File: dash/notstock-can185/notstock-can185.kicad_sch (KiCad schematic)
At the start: 29 parts, among them J1 OBD 12V GND H L, J2 UART wires from display, J3 BAT to display, U1 LMR16006YDDCR, U2 SN65HVD230

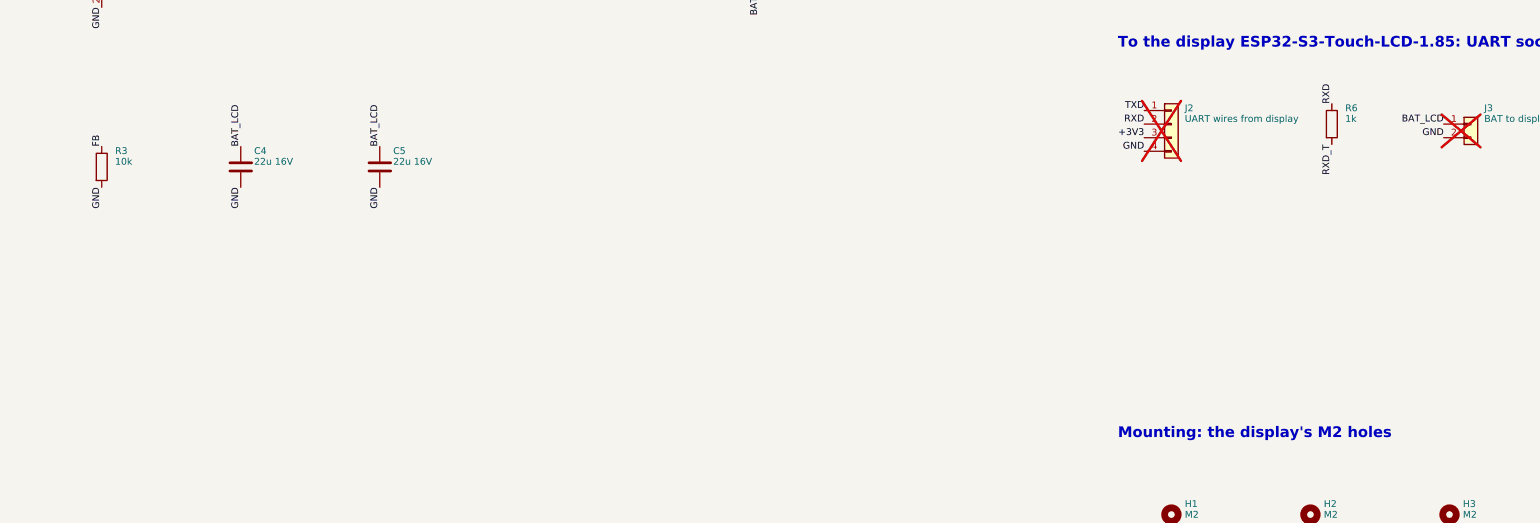
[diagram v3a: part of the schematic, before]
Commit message: CAN 1.85 rev 7: LC filter on the display's supply, JST XH for J1
Rev 6 in the car: the display's touch needed a hard press. A second LC
stage after the regulator (L2 1 uH, C9 C10 22 uF, C11 100 nF), its
corner about 30 kHz, keeps the 2.1 MHz ripple some 70 dB lower off the
display; the feedback stays before it. L2 about 12 mm from L1.

J1 is a JST XH 2.5 mm (B4B-XH-A, C144395, through hole): bigger crimps
than the PH, ready-made leads. The T5 vent's lid has its window moved
and grown for it. Readable schematic: D1 and D3 named as fitted.

Co-Authored-By: Claude Opus 5.5 <noreply@anthropic.com>
Claude-Session: https://claude.ai/code/session_018SKN4tJhAPpVCWtvRZgZpD
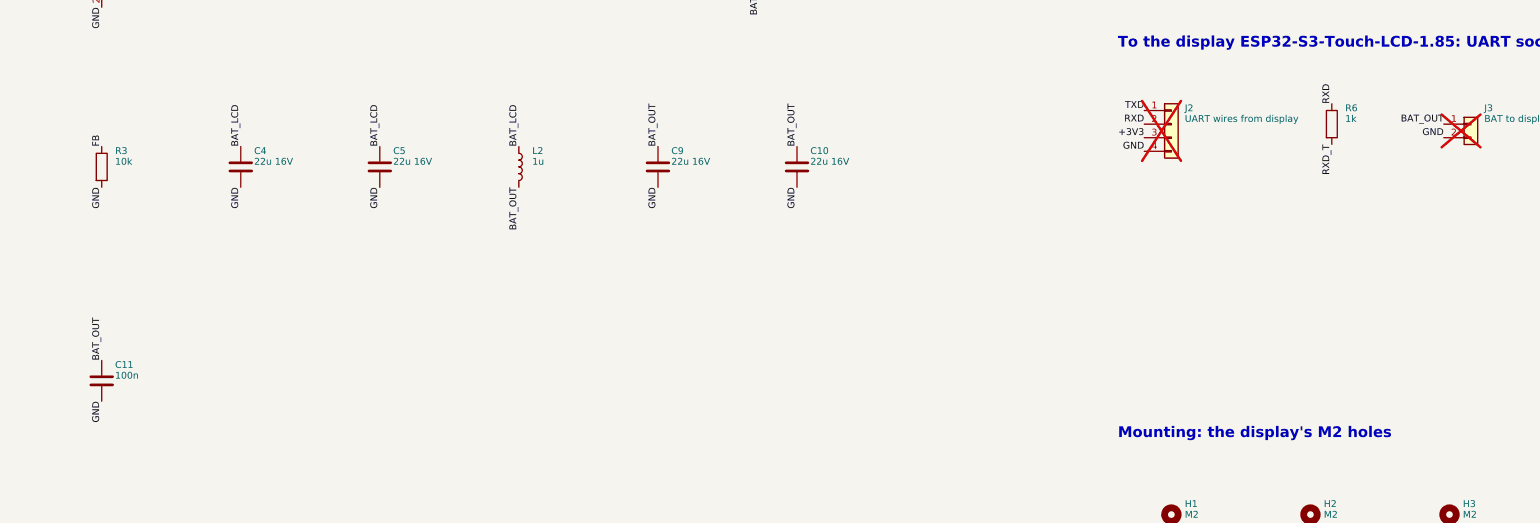
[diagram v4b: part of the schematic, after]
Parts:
- added C10, C9: 22u 16V, Capacitor_SMD:C_1206_3216Metric, symbol Device:C
- added C11: 100n, Capacitor_SMD:C_0603_1608Metric, symbol Device:C
- added L2: 1u, Inductor_SMD:L_Sunlord_SWPA4026S, symbol Device:L
- J1: footprint Connector_JST:JST_PH_B4B-PH-SM4-TB_1x04-1MP_P2.00mm_Vertical -> Connector_JST:JST_XH_B4B-XH-A_1x04_P2.50mm_Vertical; LCSC C160354 -> C144395; MPN JST B4B-PH-SM4-TB(LF)(SN) -> JST B4B-XH-A(LF)(SN)
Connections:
- net BAT_LCD: now also L2.1; no longer J3.1 (Pin_1)
- net GND: now also C10.2, C11.2, C9.2
- new net BAT_OUT: C10.1, C11.1, C9.1, J3.1 (Pin_1), L2.2
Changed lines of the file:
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@@
   (title_block
     (title "NOT STOCK CAN 1.85")
-    (rev "6")
+    (rev "7")
     (comment 1 "12 V -> 3.75 V, CAN (SN65HVD230) for the round gauge")
   )
@@
     (property "Value" "OBD 12V GND H L" (at 32.5 49 0)
       (effects (font (size 1.27 1.27)) (justify left)))
-    (property "Footprint" "Connector_JST:JST_PH_B4B-PH-SM4-TB_1x04-1MP_P2.00mm_Vertical" (at 30 50 0)
+    (property "Footprint" "Connector_JST:JST_XH_B4B-XH-A_1x04_P2.50mm_Vertical" (at 30 50 0)
       (effects (font (size 1.27 1.27)) hide))
     (property "Datasheet" "~" (at 30 50 0)
       (effects (font (size 1.27 1.27)) hide))
-    (property "LCSC" "C160354" (at 30 50 0)
-      (effects (font (size 1.27 1.27)) hide))
-    (property "MPN" "JST B4B-PH-SM4-TB(LF)(SN)" (at 30 50 0)
+    (property "LCSC" "C144395" (at 30 50 0)
+      (effects (font (size 1.27 1.27)) hide))
+    (property "MPN" "JST B4B-XH-A(LF)(SN)" (at 30 50 0)
       (effects (font (size 1.27 1.27)) hide))
     (pin "1")
@@
   )
   (label "GND" (at 82 183.81 270) (fields_autoplaced)
+    (effects (font (size 1.27 1.27)) (justify right bottom))
+  )
+  (symbol (lib_id "Device:L") (at 108 180 0) (unit 1)
+    (in_bom yes) (on_board yes) (dnp no)
+    (property "Reference" "L2" (at 110.5 177 0)
+      (effects (font (size 1.27 1.27)) (justify left)))
+    (property "Value" "1u" (at 110.5 179 0)
+      (effects (font (size 1.27 1.27)) (justify left)))
+    (property "Footprint" "Inductor_SMD:L_Sunlord_SWPA4026S" (at 108 180 0)
+      (effects (font (size 1.27 1.27)) hide))
+    (property "Datasheet" "~" (at 108 180 0)
+      (effects (font (size 1.27 1.27)) hide))
+    (property "LCSC" "C96890" (at 108 180 0)
+      (effects (font (size 1.27 1.27)) hide))
+    (property "MPN" "Sunlord SWPA4026S1R0NT (1 uH 3 A)" (at 108 180 0)
+      (effects (font (size 1.27 1.27)) hide))
+    (pin "1")
+    (pin "2")
+    (instances
+      (project "notstock-can185"
+        (path "/04b217bf-ab66-52c3-847c-db755251132b"
+          (reference "L2") (unit 1)
+        )
+      )
+    )
+  )
+  (label "BAT_LCD" (at 108 176.19 90) (fields_autoplaced)
+    (effects (font (size 1.27 1.27)) (justify left bottom))
+  )
+  (label "BAT_OUT" (at 108 183.81 270) (fields_autoplaced)
+    (effects (font (size 1.27 1.27)) (justify right bottom))
+  )
+  (symbol (lib_id "Device:C") (at 134 180 0) (unit 1)
+    (in_bom yes) (on_board yes) (dnp no)
+    (property "Reference" "C9" (at 136.5 177 0)
+      (effects (font (size 1.27 1.27)) (justify left)))
+    (property "Value" "22u 16V" (at 136.5 179 0)
+      (effects (font (size 1.27 1.27)) (justify left)))
+    (property "Footprint" "Capacitor_SMD:C_1206_3216Metric" (at 134 180 0)
+      (effects (font (size 1.27 1.27)) hide))
+    (property "Datasheet" "~" (at 134 180 0)
+      (effects (font (size 1.27 1.27)) hide))
+    (property "LCSC" "C90146" (at 134 180 0)
+      (effects (font (size 1.27 1.27)) hide))
+    (property "MPN" "Samsung CL31A226KOHNNNE (22 uF 16 V X5R 1206)" (at 134 180 0)
+      (effects (font (size 1.27 1.27)) hide))
+    (pin "1")
+    (pin "2")
+    (instances
+      (project "notstock-can185"
+        (path "/04b217bf-ab66-52c3-847c-db755251132b"
+          (reference "C9") (unit 1)
+        )
+      )
+    )
+  )
+  (label "BAT_OUT" (at 134 176.19 90) (fields_autoplaced)
+    (effects (font (size 1.27 1.27)) (justify left bottom))
+  )
+  (label "GND" (at 134 183.81 270) (fields_autoplaced)
+    (effects (font (size 1.27 1.27)) (justify right bottom))
+  )
+  (symbol (lib_id "Device:C") (at 160 180 0) (unit 1)
+    (in_bom yes) (on_board yes) (dnp no)
+    (property "Reference" "C10" (at 162.5 177 0)
+      (effects (font (size 1.27 1.27)) (justify left)))
+    (property "Value" "22u 16V" (at 162.5 179 0)
+      (effects (font (size 1.27 1.27)) (justify left)))
+    (property "Footprint" "Capacitor_SMD:C_1206_3216Metric" (at 160 180 0)
+      (effects (font (size 1.27 1.27)) hide))
+    (property "Datasheet" "~" (at 160 180 0)
+      (effects (font (size 1.27 1.27)) hide))
+    (property "LCSC" "C90146" (at 160 180 0)
+      (effects (font (size 1.27 1.27)) hide))
+    (property "MPN" "Samsung CL31A226KOHNNNE (22 uF 16 V X5R 1206)" (at 160 180 0)
+      (effects (font (size 1.27 1.27)) hide))
+    (pin "1")
+    (pin "2")
+    (instances
+      (project "notstock-can185"
+        (path "/04b217bf-ab66-52c3-847c-db755251132b"
+          (reference "C10") (unit 1)
+        )
+      )
+    )
+  )
+  (label "BAT_OUT" (at 160 176.19 90) (fields_autoplaced)
+    (effects (font (size 1.27 1.27)) (justify left bottom))
+  )
+  (label "GND" (at 160 183.81 270) (fields_autoplaced)
+    (effects (font (size 1.27 1.27)) (justify right bottom))
+  )
+  (symbol (lib_id "Device:C") (at 30 220 0) (unit 1)
+    (in_bom yes) (on_board yes) (dnp no)
+    (property "Reference" "C11" (at 32.5 217 0)
+      (effects (font (size 1.27 1.27)) (justify left)))
+    (property "Value" "100n" (at 32.5 219 0)
+      (effects (font (size 1.27 1.27)) (justify left)))
+    (property "Footprint" "Capacitor_SMD:C_0603_1608Metric" (at 30 220 0)
+      (effects (font (size 1.27 1.27)) hide))
+    (property "Datasheet" "~" (at 30 220 0)
+      (effects (font (size 1.27 1.27)) hide))
+    (property "LCSC" "C14663" (at 30 220 0)
+      (effects (font (size 1.27 1.27)) hide))
+    (property "MPN" "YAGEO CC0603KRX7R9BB104 (100 nF 50 V)" (at 30 220 0)
+      (effects (font (size 1.27 1.27)) hide))
+    (pin "1")
+    (pin "2")
+    (instances
+      (project "notstock-can185"
+        (path "/04b217bf-ab66-52c3-847c-db755251132b"
+          (reference "C11") (unit 1)
+        )
+      )
+    )
+  )
+  (label "BAT_OUT" (at 30 216.19 90) (fields_autoplaced)
+    (effects (font (size 1.27 1.27)) (justify left bottom))
+  )
+  (label "GND" (at 30 223.81 270) (fields_autoplaced)
     (effects (font (size 1.27 1.27)) (justify right bottom))
   )
@@
     )
   )
-  (label "BAT_LCD" (at 280.92 172 180) (fields_autoplaced)
-    (effects (font (size 1.27 1.27)) (justify right bottom))
-  )
+  (label "BAT_OUT" (at 280.92 172 180) (fields_autoplaced)
+    (effects (font (size 1.27 1.27)) (justify right bottom))
+  )
